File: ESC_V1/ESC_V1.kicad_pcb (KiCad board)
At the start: 2 copper layers, 63 x 22.2 mm, 19 parts, among them J1 Conn_01x07_Female, J2 Conn_01x01_Female, J3 Conn_01x01_Female, J4 Conn_01x01_Female, J5 Conn_01x01_Female, J6 Conn_01x01_Female, Q11 P Channel 40V 30A, Q12 N Channel 40V 30A, Q3 P Channel 40V 30A, Q4 N Channel 40V 30A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

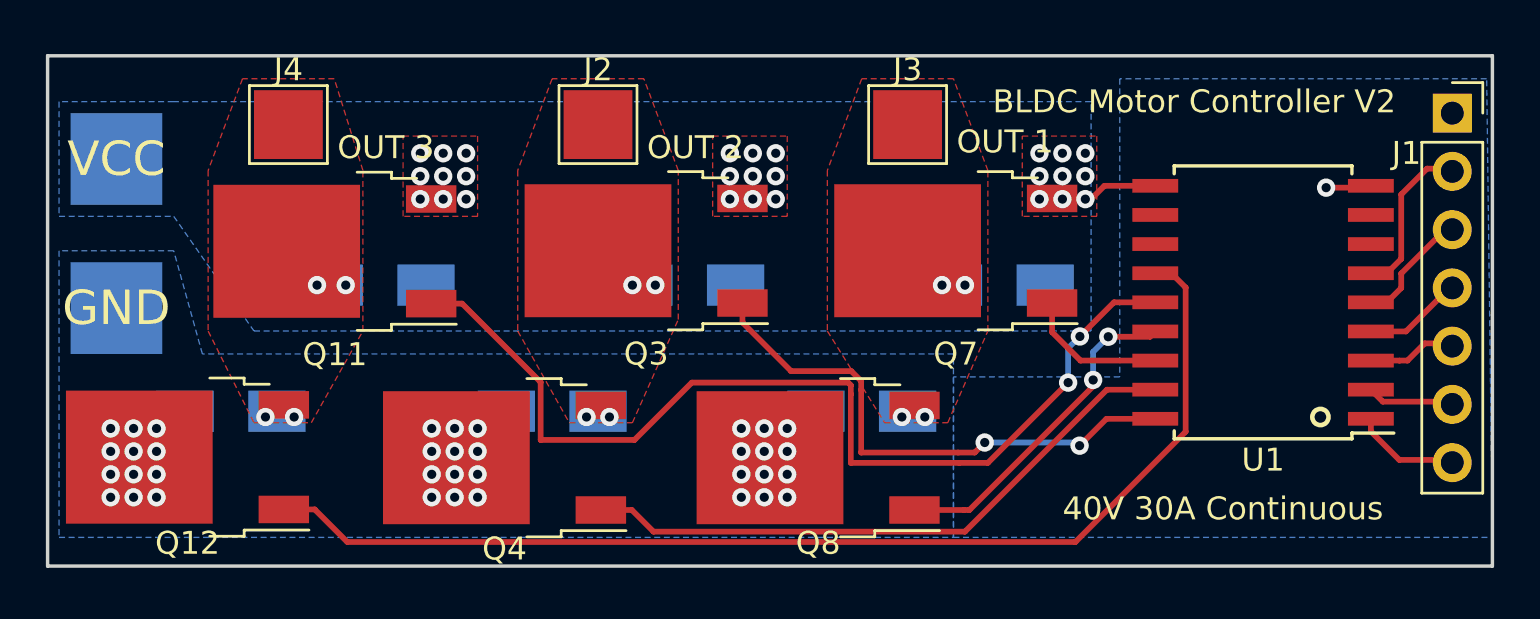
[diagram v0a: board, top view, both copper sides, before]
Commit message: FETs moved but no bridge drivers yet
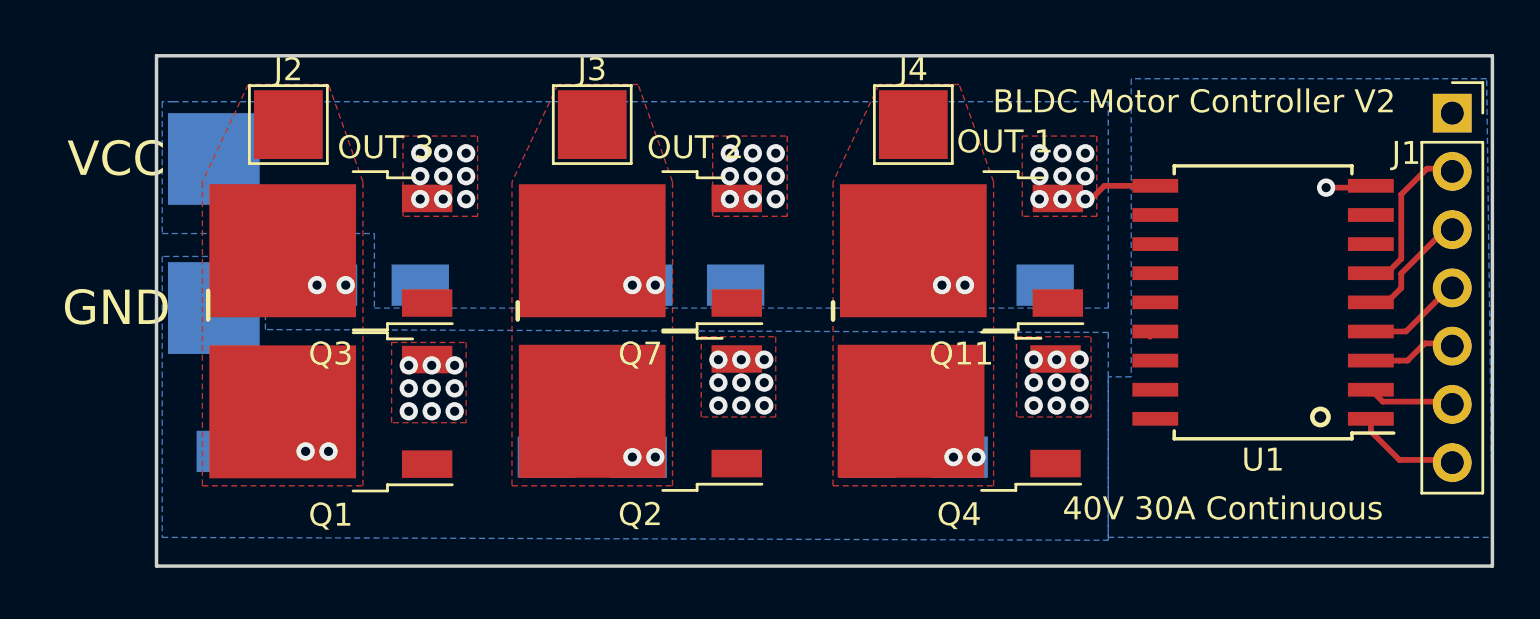
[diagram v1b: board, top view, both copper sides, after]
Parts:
- removed Q12, Q8: N Channel 40V 30A, Package_TO_SOT_SMD:TO-252-2
- added Q1: BSP129, Package_TO_SOT_SMD:TO-252-2, F.Cu at (134.3, 64.0)
- added Q2: BSP129, Package_TO_SOT_SMD:TO-252-2, F.Cu at (147.8, 64.0)
- Q4: value N Channel 40V 30A -> BSP129
- moved D6 29.8 mm to (159.8, 66.0)
- moved Q11 27.3 mm to (161.8, 57.0)
- moved J4 27.2 mm to (159.8, 51.5)
- moved D5 27.0 mm to (163.5, 58.5)
- moved Q4 19.9 mm to (161.8, 64.0)
- moved D1 13.8 mm to (136.2, 58.5)
- moved J3 13.8 mm to (145.8, 51.5)
- moved Q3 13.8 mm to (134.3, 57.0)
- moved Q7 13.8 mm to (147.8, 57.0)
- moved D3 13.5 mm to (150.0, 58.5)
- moved J2 13.5 mm to (132.5, 51.5)
- moved D2 12.4 mm to (131.8, 65.8)
- moved D4 11.9 mm to (145.8, 66.0)
- moved J5 4.25 mm to (129.2, 53.0)
- moved J6 4.25 mm to (129.2, 59.5)
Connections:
- Q4 pad 1: OUT2 -> OUT6
- Q4 pad 2: GND -> MOTOR3
- Q4 pad 3: MOTOR1 -> GND
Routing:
- net OUT6: track 49.8 -> 0.00 mm
- net OUT5: track 43.8 -> 0.00 mm, vias 2 -> 0
- net OUT2: track 27.1 -> 0.00 mm
- net OUT1: track 23.7 -> 0.00 mm, vias 2 -> 0
- net OUT4: track 14.6 -> 0.33 mm, vias 2 -> 0
- net OUT3: track 6.28 -> 0.00 mm
- net GND: vias 37 -> 28
- added copper zone on F.Cu, net GND
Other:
- board size 63 x 22.2 mm -> 58.2 x 22.2 mm

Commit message: Fixing git issues
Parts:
- added R1: 100 ohm, Resistor_SMD:R_0603_1608Metric_Pad1.05x0.95mm_HandSolder, B.Cu at (176.2, 64.2)
- added R2: 100 ohm, Resistor_SMD:R_0603_1608Metric_Pad1.05x0.95mm_HandSolder, B.Cu at (176.2, 62.8)
- added R3: 100 ohm, Resistor_SMD:R_0603_1608Metric_Pad1.05x0.95mm_HandSolder, B.Cu at (176.2, 61.2)
- added R4: 100 ohm, Resistor_SMD:R_0603_1608Metric_Pad1.05x0.95mm_HandSolder, B.Cu at (176.2, 59.8)
- added R5: 100 ohm, Resistor_SMD:R_0603_1608Metric_Pad1.05x0.95mm_HandSolder, B.Cu at (176.2, 58.2)
- added R6: 100 ohm, Resistor_SMD:R_0603_1608Metric_Pad1.05x0.95mm_HandSolder, B.Cu at (176.2, 56.8)
- moved D2 8.34 mm to (140.0, 67.0), turned to 0 degrees
- moved D4 6.08 mm to (151.8, 67.0), turned to 0 degrees
- moved J5 5.26 mm to (134.5, 52.8)
- moved J6 5.25 mm to (134.5, 59.5)
- moved D1 5.00 mm to (141.2, 58.5)
- moved D6 4.12 mm to (163.8, 67.0), turned to 0 degrees
- moved Q1 3.51 mm to (137.8, 64.3)
- moved Q3 3.51 mm to (137.8, 57.2)
- moved J2 3.50 mm to (136.0, 51.5)
- moved J3 2.00 mm to (147.8, 51.5)
- moved Q2 2.00 mm to (149.8, 64.0)
- moved Q7 2.00 mm to (149.8, 57.0)
- moved D3 1.75 mm to (151.8, 58.5)
- moved D5 0.50 mm to (164.0, 58.5)
- moved J1 0.50 mm to (182.8, 51.0)
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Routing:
- net OUT1: track 0.00 -> 48.9 mm, vias 0 -> 1
- net OUT2: track 0.00 -> 38.8 mm, vias 0 -> 1
- net OUT3: track 0.00 -> 38.6 mm, vias 0 -> 1
- net OUT4: track 0.33 -> 29.2 mm, vias 0 -> 1
- net OUT6: track 0.00 -> 20.9 mm, vias 0 -> 1
- net OUT5: track 0.00 -> 9.68 mm, vias 0 -> 1
- net GND: track 1.98 -> 5.39 mm, vias 28 -> 27
- net VCC: track 4.29 -> 2.07 mm, vias 27 -> 28
- net Net-(J1-Pad2): track 7.08 -> 5.91 mm
- net Net-(J1-Pad7): track 4.61 -> 3.53 mm
- net Net-(J1-Pad4): track 4.39 -> 3.55 mm
- net Net-(J1-Pad5): track 3.86 -> 3.02 mm
- net Net-(J1-Pad6): track 3.77 -> 3.00 mm
- net Net-(J1-Pad3): track 5.28 -> 4.64 mm
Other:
- board size 58.2 x 22.2 mm -> 52 x 19.5 mm
- board text added: "1"
- board text added: "2"
- board text added: "3"
- board text added: "BLDC Motor Controller"
- board text added: "V3"
- board text removed: "BLDC Motor Controller V2"
